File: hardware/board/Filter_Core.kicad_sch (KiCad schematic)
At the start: 44 parts

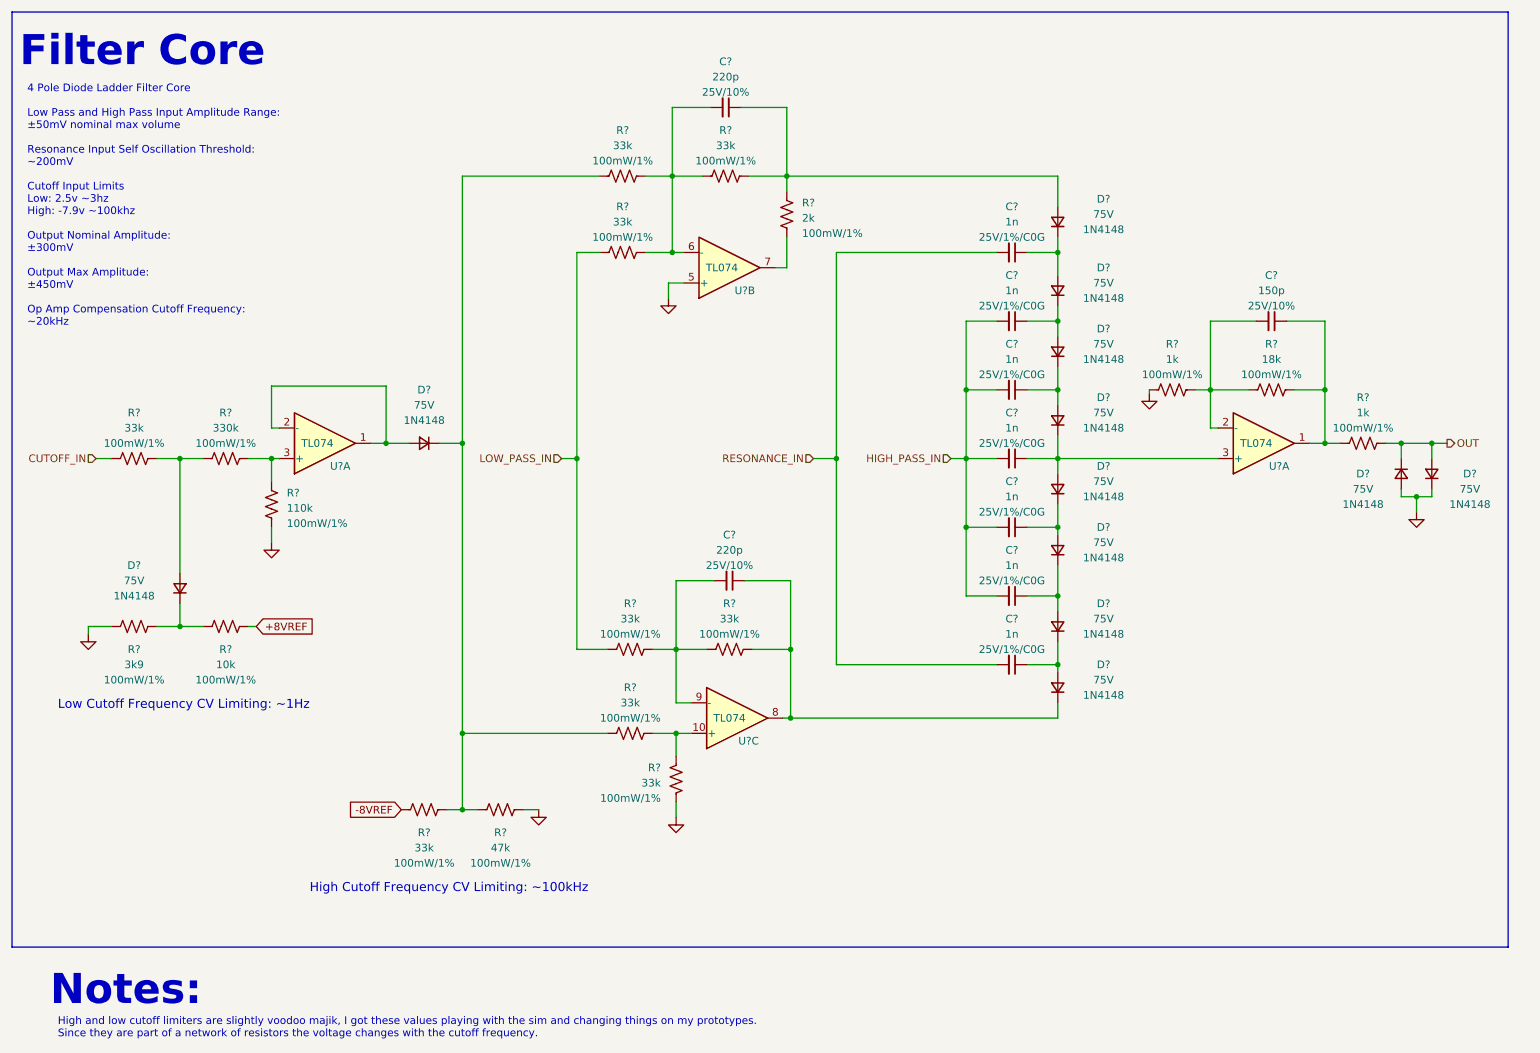
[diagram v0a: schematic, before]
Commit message: Schematic getting closer to being finished
Schematic should be close to being ready to assign MPNs.
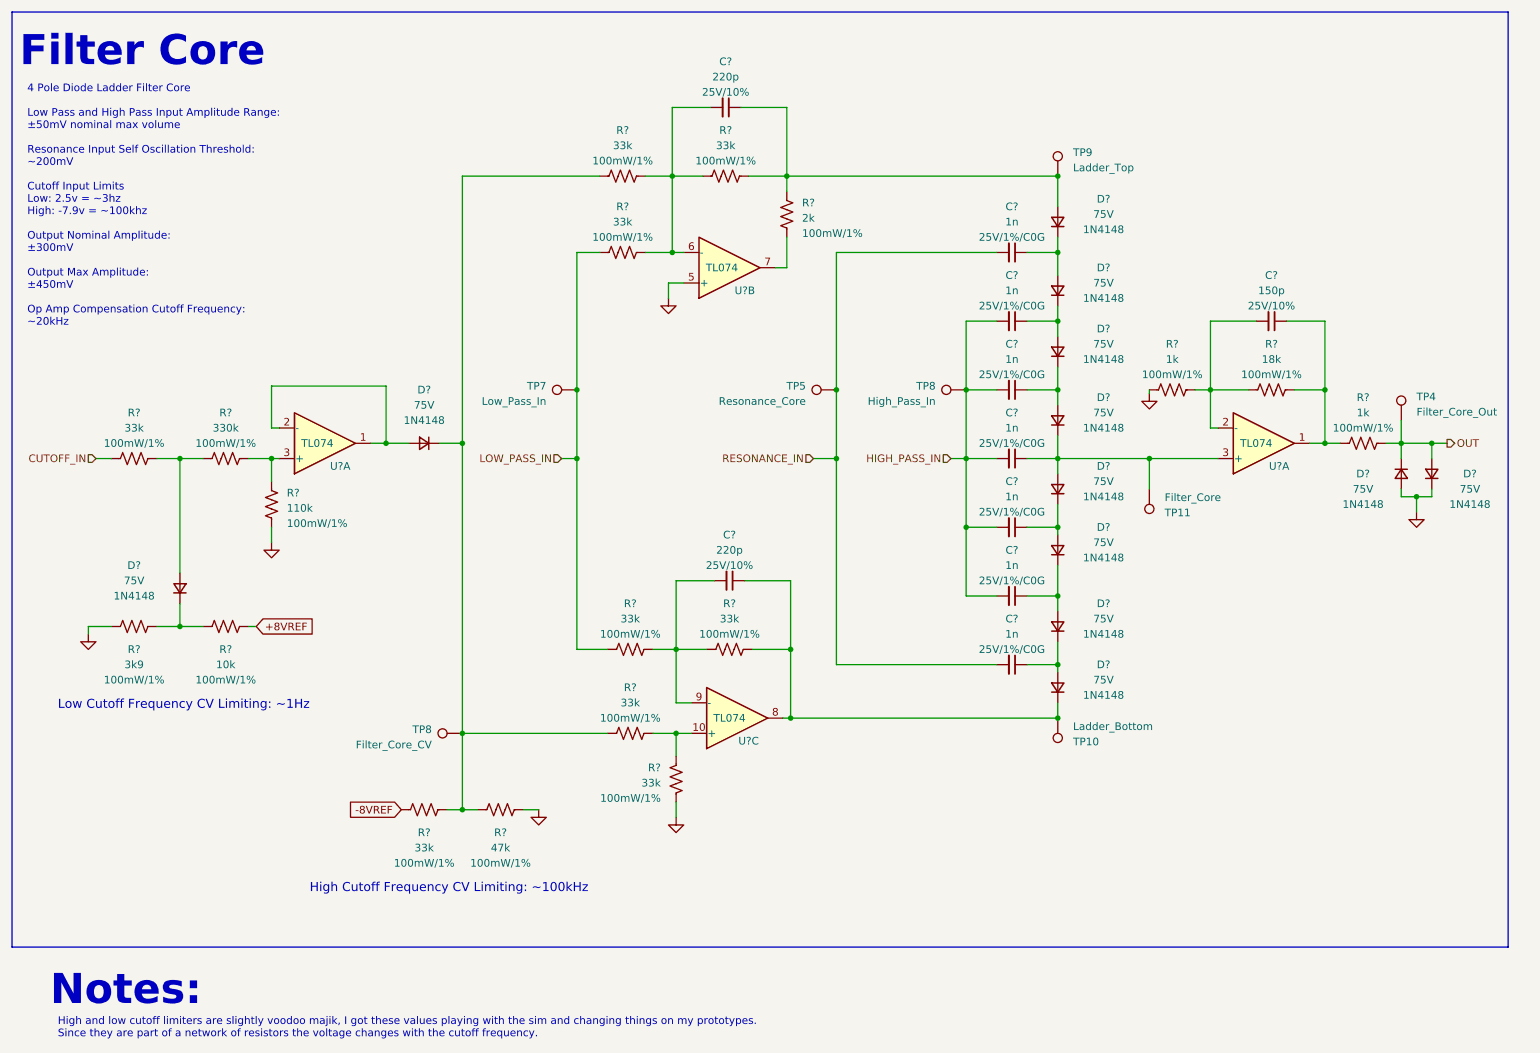
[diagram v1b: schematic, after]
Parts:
- added TP10: Ladder_Bottom, symbol Connector:TestPoint
- added TP11: Filter_Core, symbol Connector:TestPoint
- added TP4: Filter_Core_Out, symbol Connector:TestPoint
- added TP5: Resonance_Core, symbol Connector:TestPoint
- added TP7: Low_Pass_In, symbol Connector:TestPoint
- added TP8: High_Pass_In, symbol Connector:TestPoint
- added TP8: Filter_Core_CV, symbol Connector:TestPoint
- added TP9: Ladder_Top, symbol Connector:TestPoint
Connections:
- net HIGH_PASS_IN: now also TP8.1
- net LOW_PASS_IN: now also TP7.1
- net OUT: now also TP4.1
- net RESONANCE_IN: now also TP5.1
- net at D?.1 (K), R?.1, R?.2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: now also TP8.1
- net at C?.1, D?.1 (K), R?.1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: now also TP10.1
- net at C?.1, D?.2 (A), R?.1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: now also TP9.1
- net at C?.1, D?.1 (K), D?.2 (A)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: now also TP11.1
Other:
- note added: "4 Pole Diode Ladder Filter Core Low Pass and High Pass Input Amplitude Range: ±50mV nominal max volume Resonance Input Self Oscillation Threshold: ~200mV Cutoff Input Limits Low: 2.5v = ~3hz High: -7.9v = ~100khz Output Nominal Amplitude: ±300mV Output Max Amplitude: ±450mV Op Amp Compensation Cutoff Frequency: ~20kHz"
- note removed: "4 Pole Diode Ladder Filter Core Low Pass and High Pass Input Amplitude Range: ±50mV nominal max volume Resonance Input Self Oscillation Threshold: ~200mV Cutoff Input Limits Low: 2.5v ~3hz High: -7.9v ~100khz Output Nominal Amplitude: ±300mV Output Max Amplitude: ±450mV Op Amp Compensation Cutoff Frequency: ~20kHz"

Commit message: BOM Consolidation
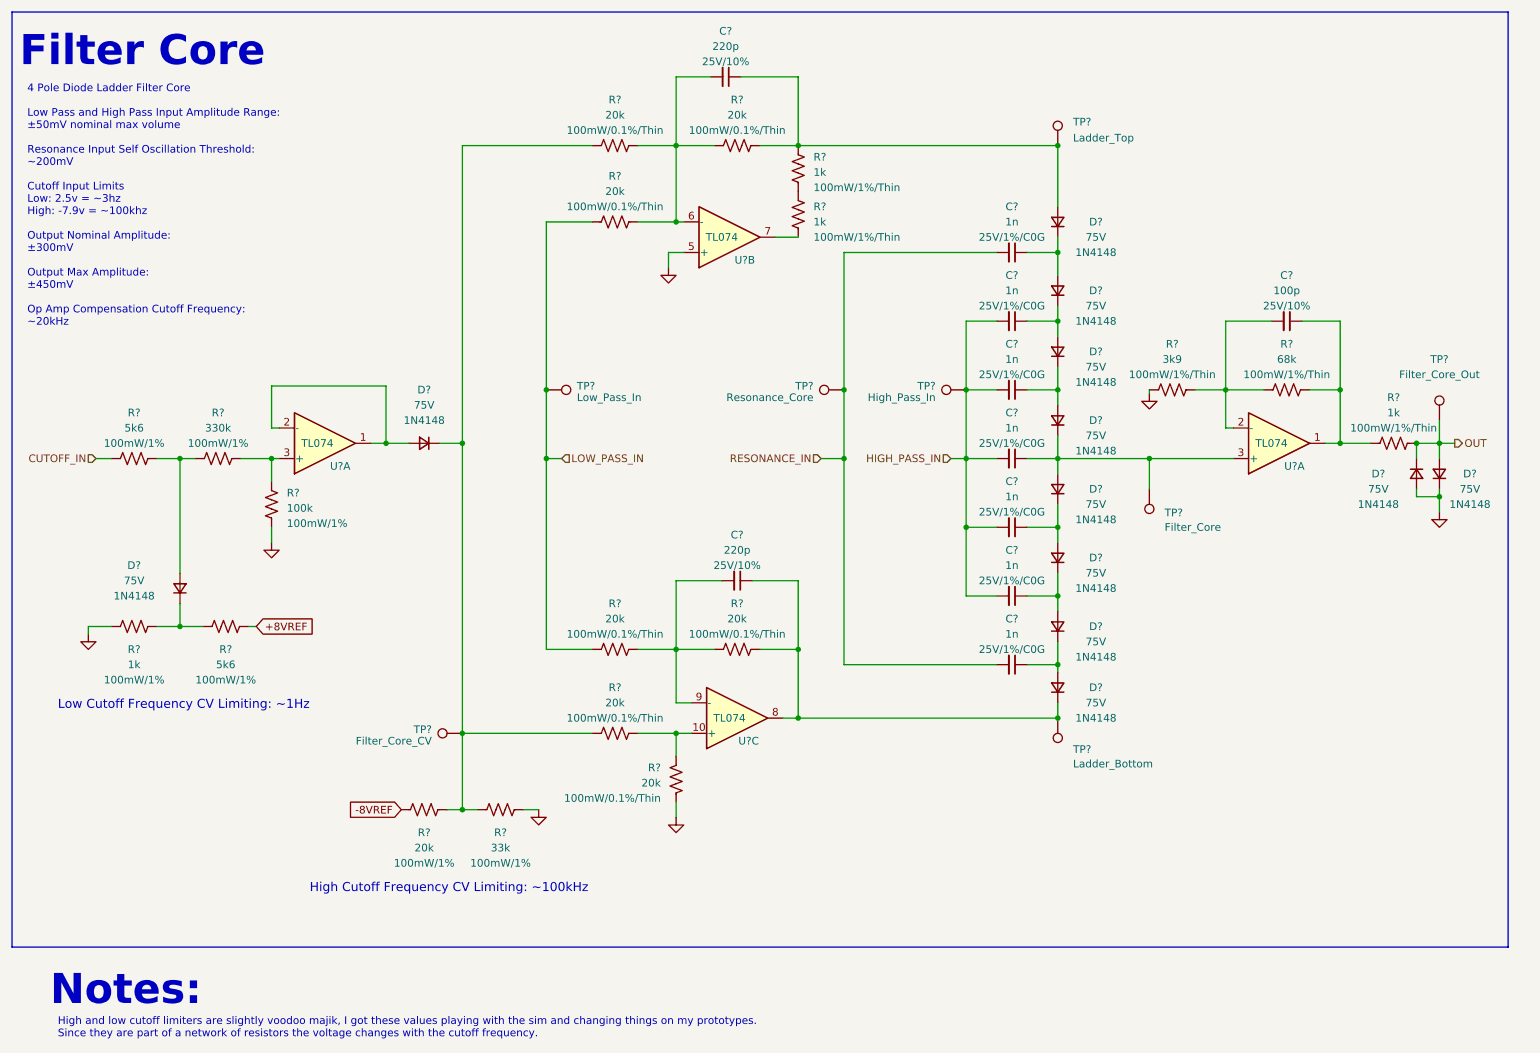
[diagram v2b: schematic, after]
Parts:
- added R?: 1k, winterbloom:R_0603_HandSolder, symbol Device:R_US
- C?: value 150p -> 100p
- R? (x7): value 33k -> 20k; Rating 100mW/1% -> 100mW/0.1%/Thin
- R?: Rating 100mW/1% -> 100mW/1%/Thin
- R?: value 47k -> 33k
- R?: value 110k -> 100k
- R?: value 1k -> 3k9; Rating 100mW/1% -> 100mW/1%/Thin
- R?: value 33k -> 20k
- R?: value 3k9 -> 1k
- R?: value 10k -> 5k6
- R?: value 2k -> 1k; Rating 100mW/1% -> 100mW/1%/Thin
- R?: value 18k -> 68k; Rating 100mW/1% -> 100mW/1%/Thin
- R?: value 33k -> 5k6
- TP?: renamed from TP5; value Resonance_Core -> ~; Name (none) -> Resonance_Core
- TP?: renamed from TP7; value Low_Pass_In -> ~; Name (none) -> Low_Pass_In
- TP?: renamed from TP11; value Filter_Core -> ~; Name (none) -> Filter_Core
- TP?: renamed from TP4; value Filter_Core_Out -> ~; Name (none) -> Filter_Core_Out
- TP?: renamed from TP8; value High_Pass_In -> ~; Name (none) -> High_Pass_In
- TP?: renamed from TP10; value Ladder_Bottom -> ~; Name (none) -> Ladder_Bottom
- TP?: renamed from TP8; value Filter_Core_CV -> ~; Name (none) -> Filter_Core_CV
- TP?: renamed from TP9; value Ladder_Top -> ~; Name (none) -> Ladder_Top
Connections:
- net at U?.7: now also R?.2; no longer R?.2
- new net: R?.1, R?.2
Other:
- moved on the sheet: C?, D?, R?, TP?, U?A, U?B

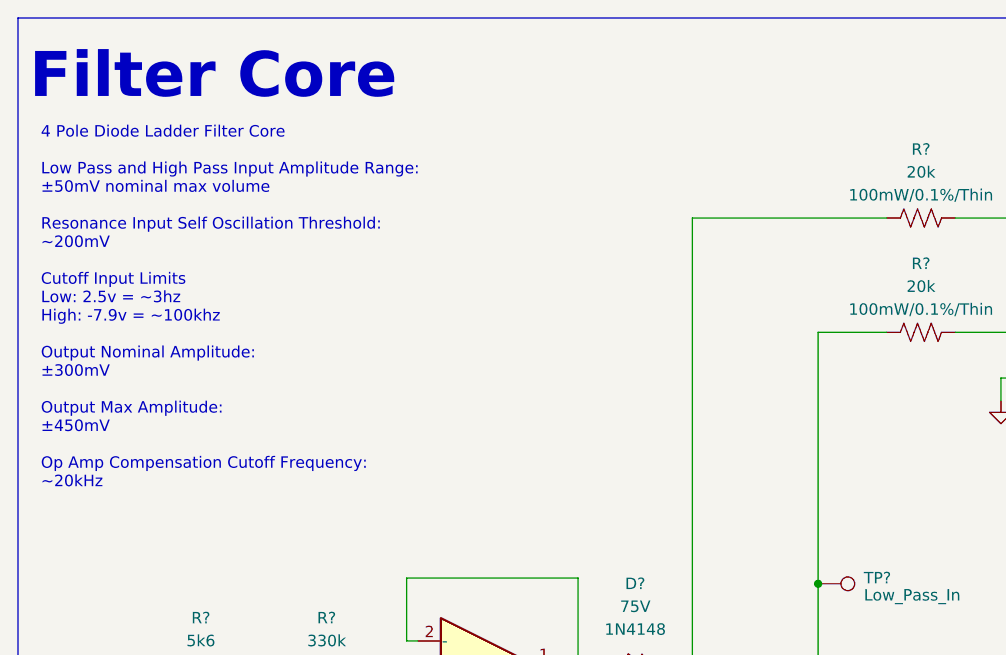
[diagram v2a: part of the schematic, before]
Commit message: Updates for LED Drivers
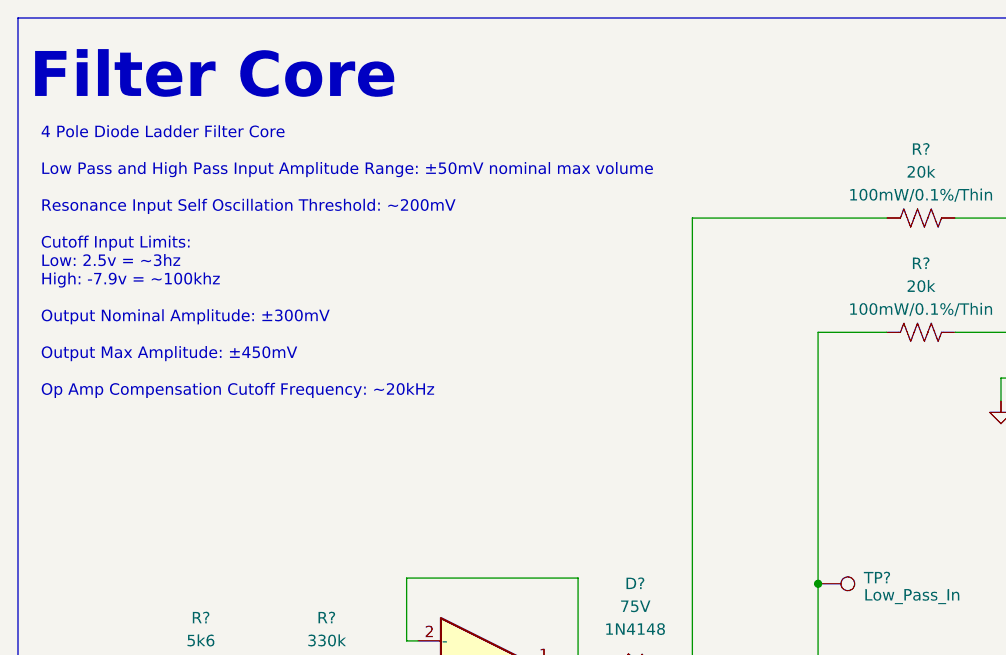
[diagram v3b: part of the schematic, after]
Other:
- note added: "4 Pole Diode Ladder Filter Core Low Pass and High Pass Input Amplitude Range: ±50mV nominal max volume Resonance Input Self Oscillation Threshold: ~200mV Cutoff Input Limits: Low: 2.5v = ~3hz High: -7.9v = ~100khz Output Nominal Amplitude: ±300mV Output Max Amplitude: ±450mV Op Amp Compensation Cutoff Frequency: ~20kHz"
- note removed: "4 Pole Diode Ladder Filter Core Low Pass and High Pass Input Amplitude Range: ±50mV nominal max volume Resonance Input Self Oscillation Threshold: ~200mV Cutoff Input Limits Low: 2.5v = ~3hz High: -7.9v = ~100khz Output Nominal Amplitude: ±300mV Output Max Amplitude: ±450mV Op Amp Compensation Cutoff Frequency: ~20kHz"
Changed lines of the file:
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@@
     (effects (font (size 5 5) (thickness 0.508) bold) (justify left bottom))
   )
-  (text "4 Pole Diode Ladder Filter Core\n\nLow Pass and High Pass Input Amplitude Range:\n±50mV nominal max volume\n\nResonance Input Self Oscillation Threshold:\n~200mV\n\nCutoff Input Limits\nLow: 2.5v = ~3hz\nHigh: -7.9v = ~100khz\n\nOutput Nominal Amplitude:\n±300mV\n\nOutput Max Amplitude:\n±450mV\n\nOp Amp Compensation Cutoff Frequency:\n~20kHz\n\n\n"
-    (at 17.78 71.12 0)
+  (text "4 Pole Diode Ladder Filter Core\n\nLow Pass and High Pass Input Amplitude Range: ±50mV nominal max volume\n\nResonance Input Self Oscillation Threshold: ~200mV\n\nCutoff Input Limits:\nLow: 2.5v = ~3hz\nHigh: -7.9v = ~100khz\n\nOutput Nominal Amplitude: ±300mV\n\nOutput Max Amplitude: ±450mV\n\nOp Amp Compensation Cutoff Frequency: ~20kHz\n\n\n"
+    (at 17.78 60.96 0)
     (effects (font (size 1.27 1.27)) (justify left bottom))
   )

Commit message: hardware: update schematic with footprints and preliminary MPNs
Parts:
- C? (x7), R? (x17): smd kit 1 -> (none)
- C? (x3): Notes 0603, 25V+, 10% -> (none); smd kit 1 -> (none)
- D? (x9): value 75V -> BAS315; footprint Diode_SMD:D_SOD-123 -> winterbloom:D_SOD-323; LCSC C81598 -> (none); MPN 1N4148W -> BAS316,115; Manufacturer ST(Semtech) -> (none); Notes (none) -> Audio path; Rating 1N4148 -> 1Vf @ 100mA
- D? (x3): value 75V -> BAS315; footprint Diode_SMD:D_SOD-123 -> winterbloom:D_SOD-323; LCSC C81598 -> (none); MPN 1N4148W -> BAS316,115; Manufacturer ST(Semtech) -> (none); Notes (none) -> Clipping diode; Rating 1N4148 -> 1Vf @ 100mA
- R?: Rating 100mW/1% -> 100mW/1%/Thin; smd kit 1 -> (none)
- R?: Rating 100mW/1% -> 100mW/0.1%/Thin; smd kit 1 -> (none)
- TP505, TP506, TP507, TP508: renamed from TP?; footprint (none) -> TestPoint:TestPoint_Pad_D1.5mm
- TP? (x4): footprint (none) -> TestPoint:TestPoint_Pad_D1.5mm
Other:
- title: Diode Ladder Filter -> Neptune

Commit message: Very first component layout.
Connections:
- net GND: now also U?.3 (+); no longer U?.5 (+)
- net at R?.1, R?.2: now also U?.5 (+); no longer U?.10 (+)
- net at C?.1, D?.1 (K), R?.1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: now also U?.7; no longer U?.8
- net at C?.2, R?.1, R?.2: now also U?.6 (-); no longer U?.9 (-)
- net at C?.1, R?.1, R?.2: now also U?.8; no longer U?.1
- net at C?.2, R?.1, R?.1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: now also U?.2 (-); no longer U?.6 (-)
- net at C?.1, D?.1 (K), D?.2 (A)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: now also U?.10 (+); no longer U?.3 (+)
- net at R?.1, R?.1: now also U?.3 (+); no longer U?.3 (+)
- net at R?.2: now also U?.1; no longer U?.7
- net at C?.2, R?.1, R?.2: now also U?.9 (-); no longer U?.2 (-)
- new net: D?.2 (A), U?.1, U?.2 (-)
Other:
- moved on the sheet: C?, U?A, U?B, U?C
